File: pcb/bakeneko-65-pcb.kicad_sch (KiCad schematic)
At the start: 18 parts, among them J1 JST SH 4-pin, J2 AVR-ISP-6, SW1 Reset, U1 SRV05-4, U2 ATmega32U4-M, Y1 16MHz

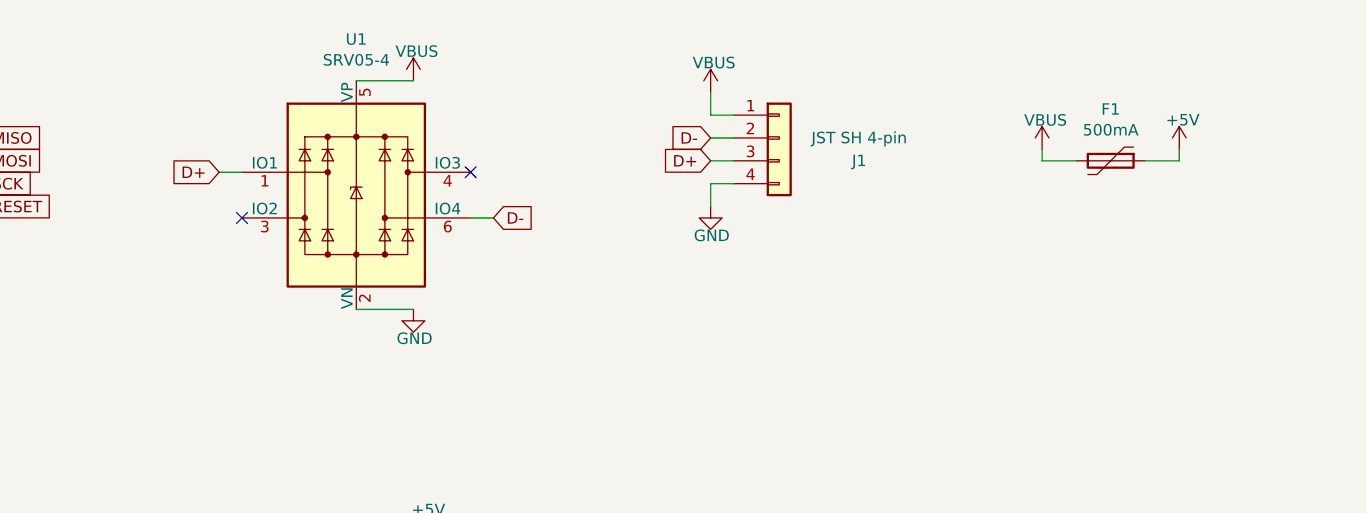
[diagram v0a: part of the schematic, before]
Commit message: USB Trace routing updates
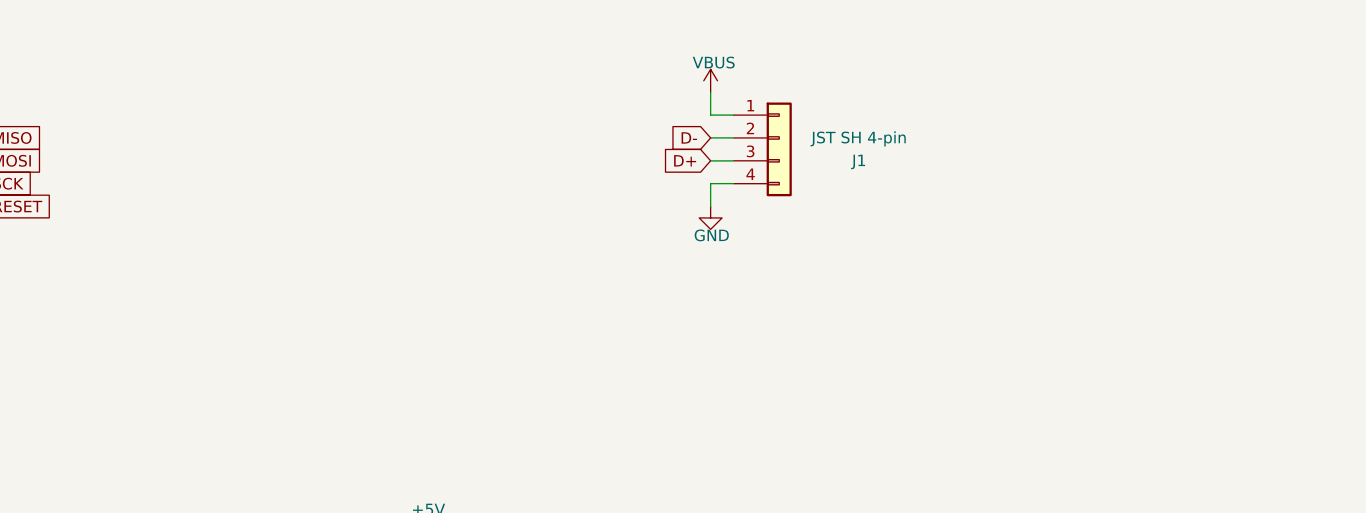
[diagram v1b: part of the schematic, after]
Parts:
- removed F1: 500mA, Fuse:Fuse_1206_3216Metric, symbol Device:Polyfuse
- removed U1: SRV05-4, Package_TO_SOT_SMD:SOT-23-6, symbol Power_Protection:SRV05-4
- R2, R3: footprint Resistor_SMD:R_0603_1608Metric -> Resistor_SMD:R_0402_1005Metric
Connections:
- no-connect marks 4 -> 2

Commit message: Trace updates
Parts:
- R2, R3: footprint Resistor_SMD:R_0402_1005Metric -> Resistor_SMD:R_0603_1608Metric
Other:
- moved on the sheet: C1, C2, C3, C4, C5, C6, C7, J1, R1, R2, R3, R4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

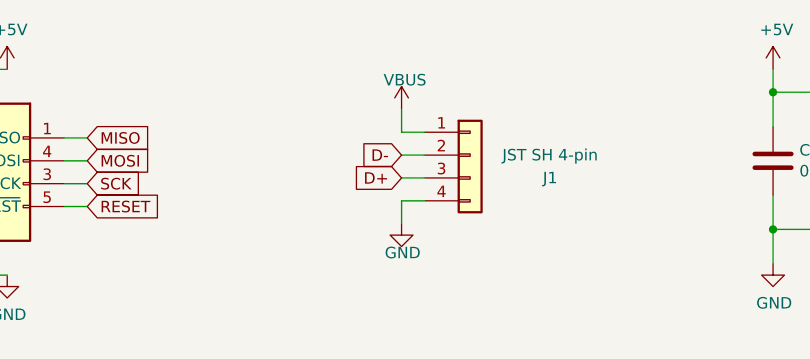
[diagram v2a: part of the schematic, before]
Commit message: Edge cut update, generate Gerber files
Updated the edge cuts to be closer to the Iron165 PCB, did some additional trace cleanup, and generated the Gerber, BOM, and positioning files.
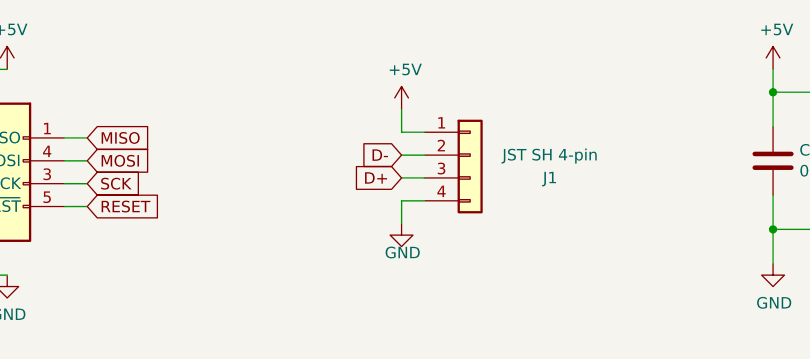
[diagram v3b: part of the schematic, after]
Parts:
- C1, C2, C3: LCSC Part # C49678 -> C14663
- C4: LCSC Part # C15850 -> C19702
- C5, C6: LCSC Part # C1804 -> C1653
- C7: LCSC Part # C28323 -> C15849
- R1, R4: LCSC Part # C17414 -> C25804
- R2, R3: LCSC Part # C17561 -> C23345
- U2: LCSC Part # (none) -> C112161
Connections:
- net +5V: now also J1.1 (Pin_1)
- net VBUS: no longer J1.1 (Pin_1)
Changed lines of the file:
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@@
       (effects (font (size 1.27 1.27)) hide)
     )
-    (property "LCSC Part #" "C49678" (id 4) (at 140.97 40.64 0)
+    (property "LCSC Part #" "C14663" (id 4) (at 140.97 40.64 0)
       (effects (font (size 1.27 1.27)) hide)
     )
@@
       (effects (font (size 1.27 1.27)) hide)
     )
-    (property "LCSC Part #" "C49678" (id 4) (at 151.13 40.64 0)
+    (property "LCSC Part #" "C14663" (id 4) (at 151.13 40.64 0)
       (effects (font (size 1.27 1.27)) hide)
     )
@@
       (effects (font (size 1.27 1.27)) hide)
     )
-    (property "LCSC Part #" "C49678" (id 4) (at 161.29 40.64 0)
+    (property "LCSC Part #" "C14663" (id 4) (at 161.29 40.64 0)
       (effects (font (size 1.27 1.27)) hide)
     )
@@
       (effects (font (size 1.27 1.27)) hide)
     )
-    (property "LCSC Part #" "C15850" (id 4) (at 171.45 40.64 0)
+    (property "LCSC Part #" "C19702" (id 4) (at 171.45 40.64 0)
       (effects (font (size 1.27 1.27)) hide)
     )
@@
       (effects (font (size 1.27 1.27)) hide)
     )
-    (property "LCSC Part #" "C17561" (id 4) (at 35.56 116.205 0)
+    (property "LCSC Part #" "C23345" (id 4) (at 35.56 116.205 0)
       (effects (font (size 1.27 1.27)) hide)
     )
@@
       (effects (font (size 1.27 1.27)) hide)
     )
-    (property "LCSC Part #" "C17561" (id 4) (at 35.56 118.745 0)
-      (effects (font (size 1.27 1.27)) hide)
-    )
-    (pin "1")
-    (pin "2")
-  )
-  (symbol (lib_id "power:VBUS") (at 99.695 34.925 0) (unit 1)
-    (in_bom yes) (on_board yes)
-    (property "Reference" "#PWR08" (id 0) (at 99.695 38.735 0)
-      (effects (font (size 1.27 1.27)) hide)
-    )
-    (property "Value" "VBUS" (id 1) (at 100.076 31.6738 0))
-    (property "Footprint" "" (id 2) (at 99.695 34.925 0)
-      (effects (font (size 1.27 1.27)) hide)
-    )
-    (property "Datasheet" "" (id 3) (at 99.695 34.925 0)
-      (effects (font (size 1.27 1.27)) hide)
-    )
-    (pin "1")
+    (property "LCSC Part #" "C23345" (id 4) (at 35.56 118.745 0)
+      (effects (font (size 1.27 1.27)) hide)
+    )
+    (pin "1")
+    (pin "2")
   )
   (symbol (lib_id "power:VBUS") (at 249.555 44.45 0) (unit 1)
@@
       (effects (font (size 1.27 1.27)) hide)
     )
-    (property "LCSC Part #" "C17414" (id 4) (at 205.74 36.83 0)
+    (property "LCSC Part #" "C25804" (id 4) (at 205.74 36.83 0)
       (effects (font (size 1.27 1.27)) hide)
     )
@@
       (effects (font (size 1.27 1.27)) hide)
     )
-    (property "LCSC Part #" "C28323" (id 4) (at 45.72 127.635 0)
+    (property "LCSC Part #" "C15849" (id 4) (at 45.72 127.635 0)
       (effects (font (size 1.27 1.27)) hide)
     )
@@
       (effects (font (size 1.27 1.27)) hide)
     )
-    (property "LCSC Part #" "C17414" (id 4) (at 87.63 144.145 0)
+    (property "LCSC Part #" "C25804" (id 4) (at 87.63 144.145 0)
       (effects (font (size 1.27 1.27)) hide)
     )
@@
       (effects (font (size 1.27 1.27)) hide)
     )
-    (property "LCSC Part #" "C1804" (id 4) (at 141.605 86.995 0)
+    (property "LCSC Part #" "C1653" (id 4) (at 141.605 86.995 0)
       (effects (font (size 1.27 1.27)) hide)
     )
@@
       (effects (font (size 1.27 1.27)) hide)
     )
-    (property "LCSC Part #" "C1804" (id 4) (at 141.605 103.505 0)
+    (property "LCSC Part #" "C1653" (id 4) (at 141.605 103.505 0)
       (effects (font (size 1.27 1.27)) hide)
     )
@@
     (pin "1")
   )
+  (symbol (lib_id "power:+5V") (at 99.695 34.925 0) (unit 1)
+    (in_bom yes) (on_board yes)
+    (property "Reference" "#PWR0103" (id 0) (at 99.695 38.735 0)
+      (effects (font (size 1.27 1.27)) hide)
+    )
+    (property "Value" "+5V" (id 1) (at 100.076 30.5308 0))
+    (property "Footprint" "" (id 2) (at 99.695 34.925 0)
+      (effects (font (size 1.27 1.27)) hide)
+    )
+    (property "Datasheet" "" (id 3) (at 99.695 34.925 0)
+      (effects (font (size 1.27 1.27)) hide)
+    )
+    (pin "1")
+  )
   (symbol (lib_id "MCU_Microchip_ATmega:ATmega32U4-M") (at 66.04 128.905 0) (unit 1)
     (in_bom yes) (on_board yes) (fields_autoplaced)
@@
     )
     (property "Datasheet" "http://ww1.microchip.com/downloads/en/DeviceDoc/Atmel-7766-8-bit-AVR-ATmega16U4-32U4_Datasheet.pdf" (id 3) (at 66.04 128.905 0)
+      (effects (font (size 1.27 1.27)) hide)
+    )
+    (property "LCSC Part #" "C112161" (id 4) (at 66.04 128.905 0)
       (effects (font (size 1.27 1.27)) hide)
     )
@@
       (reference "#PWR05") (unit 1) (value "GND") (footprint "")
     )
-    (path "/00000000-0000-0000-0000-00005f275d18"
-      (reference "#PWR08") (unit 1) (value "VBUS") (footprint "")
-    )
     (path "/00000000-0000-0000-0000-00005f24cfcc"
       (reference "#PWR09") (unit 1) (value "GND") (footprint "")
@@
       (reference "#PWR0102") (unit 1) (value "+5V") (footprint "")
     )
+    (path "/1424ac55-64fa-41a8-bf55-13c4fd0bf19e"
+      (reference "#PWR0103") (unit 1) (value "+5V") (footprint "")
+    )
     (path "/00000000-0000-0000-0000-00005f3d1a13"
